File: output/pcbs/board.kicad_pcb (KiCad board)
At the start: 2 copper layers, 94 x 82 mm, 35 parts

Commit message: fillet
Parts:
- added B1: , E73:SW_TACT_ALPS_SKQGABE010, F.Cu at (204.0, 176.5)
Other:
- outline, holes or cut-outs redrawn
- net class Default added: clearance 0.2, trace_width 0.25, via_dia 0.8, via_drill 0.4

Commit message: new footprint
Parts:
- removed B1: , E73:SW_TACT_ALPS_SKQGABE010
- MCU1: value nice_nano -> (none); footprint nice_nano -> ceoloide:mcu_nice_nano
- turned MCU1 to 90 degrees
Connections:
- net P002 renamed MCU1_18
- net P009 renamed MCU1_13
- net P010 renamed MCU1_14
- net P029 renamed MCU1_19
- net P031 renamed MCU1_20
- net P106 renamed MCU1_12
- net P111 renamed MCU1_15
- net P113 renamed MCU1_16
- net P115 renamed MCU1_17
- D1 pad 1: pinky_bottom -> P100
- D1 pad 2: (no net) -> pinky_bottom
- D10 pad 1: index_thumb -> P024
- D10 pad 2: (no net) -> index_thumb
- D11 pad 1: index_bottom -> P100
- D11 pad 2: (no net) -> index_bottom
- D12 pad 1: index_home -> P011
- D12 pad 2: (no net) -> index_home
- D13 pad 1: index_top -> P104
- D13 pad 2: (no net) -> index_top
- D14 pad 1: inner_thumb -> P024
- D14 pad 2: (no net) -> inner_thumb
- D15 pad 1: inner_bottom -> P100
- D15 pad 2: (no net) -> inner_bottom
- D16 pad 1: inner_home -> P011
- D16 pad 2: (no net) -> inner_home
- D17 pad 1: inner_top -> P104
- D17 pad 2: (no net) -> inner_top
- D2 pad 1: pinky_home -> P011
- D2 pad 2: (no net) -> pinky_home
- D3 pad 1: pinky_top -> P104
- D3 pad 2: (no net) -> pinky_top
- D4 pad 1: ring_bottom -> P100
- D4 pad 2: (no net) -> ring_bottom
- D5 pad 1: ring_home -> P011
- D5 pad 2: (no net) -> ring_home
- D6 pad 1: ring_top -> P104
- D6 pad 2: (no net) -> ring_top
- D7 pad 1: middle_bottom -> P100
- D7 pad 2: (no net) -> middle_bottom
- D8 pad 1: middle_home -> P011
- D8 pad 2: (no net) -> middle_home
- D9 pad 1: middle_top -> P104
- D9 pad 2: (no net) -> middle_top
- MCU1 pad 1: P006 -> MCU1_1
- MCU1 pad 10: P011 -> MCU1_10
- MCU1 pad 11: P104 -> MCU1_11
- MCU1 pad 2: P008 -> MCU1_2
- MCU1 pad 21: VCC -> MCU1_21
- MCU1 pad 22: RST -> MCU1_22
- MCU1 pad 23: GND -> MCU1_23
- MCU1 pad 24: RAW -> MCU1_24
- MCU1 pad 3: GND -> MCU1_3
- MCU1 pad 4: GND -> MCU1_4
- MCU1 pad 5: P017 -> MCU1_5
- MCU1 pad 6: P020 -> MCU1_6
- MCU1 pad 7: P022 -> MCU1_7
- MCU1 pad 8: P024 -> MCU1_8
- MCU1 pad 9: P100 -> MCU1_9
- S1 pad 1: (no net) -> P006
- S10 pad 1: (no net) -> P020
- S11 pad 1: (no net) -> P020
- S12 pad 1: (no net) -> P020
- S13 pad 1: (no net) -> P020
- S14 pad 1: (no net) -> P022
- S15 pad 1: (no net) -> P022
- S16 pad 1: (no net) -> P022
- S17 pad 1: (no net) -> P022
- S2 pad 1: (no net) -> P006
- S3 pad 1: (no net) -> P006
- S4 pad 1: (no net) -> P008
- S5 pad 1: (no net) -> P008
- S6 pad 1: (no net) -> P008
- S7 pad 1: (no net) -> P017
- S8 pad 1: (no net) -> P017
- S9 pad 1: (no net) -> P017
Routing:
- net (no net): track 0.00 -> 337.7 mm

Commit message: final
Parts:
- added JST1: , ceoloide:battery_connector_jst_ph_2, F.Cu at (215.0, 160.8)
- added PWR1: , ceoloide:power_switch_smd_side, F.Cu at (206.5, 165.0)
- added RST1: , ceoloide:reset_switch_tht_top, F.Cu at (193.0, 164.3)
- D1, D10, D11, D12, D13, D14, D15, D16, D17, D2, D3, D4, D5, D6, D7, D8, D9: footprint ComboDiode -> ceoloide:diode_tht_sod123; moved to B.Cu
- S1, S10, S11, S12, S13, S14, S15, S16, S17, S2, S3, S4, S5, S6, S7, S8, S9: footprint PG1350 -> ceoloide:switch_gateron_ks27_ks33; moved to B.Cu
- moved D13 13.2 mm to (236.0, 117.8), turned to 90 degrees
- moved D17 13.2 mm to (254.0, 119.8), turned to 90 degrees
- moved D3 13.2 mm to (182.0, 117.8), turned to 90 degrees
- moved D6 13.2 mm to (200.0, 112.8), turned to 90 degrees
- moved D9 13.2 mm to (218.0, 109.8), turned to 90 degrees
- moved D12 12.4 mm to (236.0, 135.8), turned to 90 degrees
- moved D16 12.4 mm to (254.0, 137.8), turned to 90 degrees
- moved D2 12.4 mm to (182.0, 135.8), turned to 90 degrees
- moved D5 12.4 mm to (200.0, 130.8), turned to 90 degrees
- moved D8 12.4 mm to (218.0, 127.8), turned to 90 degrees
- moved D1 11.6 mm to (182.0, 153.8), turned to 90 degrees
- moved D11 11.6 mm to (236.0, 153.8), turned to 90 degrees
- moved D15 11.6 mm to (254.0, 155.8), turned to 90 degrees
- moved D4 11.6 mm to (200.0, 148.8), turned to 90 degrees
- moved D7 11.6 mm to (218.0, 145.8), turned to 90 degrees
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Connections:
- D1 pad 1: P100 -> P14
- D10 pad 1: P024 -> P15
- D11 pad 1: P100 -> P14
- D12 pad 1: P011 -> P16
- D13 pad 1: P104 -> P10
- D14 pad 1: P024 -> P15
- D15 pad 1: P100 -> P14
- D16 pad 1: P011 -> P16
- D17 pad 1: P104 -> P10
- D2 pad 1: P011 -> P16
- D3 pad 1: P104 -> P10
- D4 pad 1: P100 -> P14
- D5 pad 1: P011 -> P16
- D6 pad 1: P104 -> P10
- D7 pad 1: P100 -> P14
- D8 pad 1: P011 -> P16
- D9 pad 1: P104 -> P10
- S1 pad : (no net) -> pinky_bottom
- S1 pad 1: P006 -> P2
- S10 pad : (no net) -> index_thumb
- S10 pad 1: P020 -> P5
- S11 pad : (no net) -> index_bottom
- S11 pad 1: P020 -> P5
- S12 pad : (no net) -> index_home
- S12 pad 1: P020 -> P5
- S13 pad : (no net) -> index_top
- S13 pad 1: P020 -> P5
- S14 pad : (no net) -> inner_thumb
- S14 pad 1: P022 -> P6
- S15 pad : (no net) -> inner_bottom
- S15 pad 1: P022 -> P6
- S16 pad : (no net) -> inner_home
- S16 pad 1: P022 -> P6
- S17 pad : (no net) -> inner_top
- S17 pad 1: P022 -> P6
- S2 pad : (no net) -> pinky_home
- S2 pad 1: P006 -> P2
- S3 pad : (no net) -> pinky_top
- S3 pad 1: P006 -> P2
- S4 pad : (no net) -> ring_bottom
- S4 pad 1: P008 -> P3
- S5 pad : (no net) -> ring_home
- S5 pad 1: P008 -> P3
- S6 pad : (no net) -> ring_top
- S6 pad 1: P008 -> P3
- S7 pad : (no net) -> middle_bottom
- S7 pad 1: P017 -> P4
- S8 pad : (no net) -> middle_home
- S8 pad 1: P017 -> P4
- S9 pad : (no net) -> middle_top
- S9 pad 1: P017 -> P4
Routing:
- net JST1_2: track 0.00 -> 3.60 mm
- net JST1_1: track 0.00 -> 3.60 mm
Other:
- board size 94 x 82 mm -> 94 x 86 mm

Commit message: padding adjust
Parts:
- moved D17 5.00 mm to (258.0, 116.8)
- moved S17 5.00 mm to (251.0, 120.0)
- moved D16 4.47 mm to (258.0, 135.8)
- moved S16 4.47 mm to (251.0, 139.0)
- moved D13 4.24 mm to (239.0, 114.8)
- moved S13 4.24 mm to (232.0, 118.0)
- moved D15 4.12 mm to (258.0, 154.8)
- moved S15 4.12 mm to (251.0, 158.0)
- moved D14 4.00 mm to (258.0, 173.8)
- moved S14 4.00 mm to (251.0, 177.0)
- moved D12 3.61 mm to (239.0, 133.8)
- moved D9 3.61 mm to (220.0, 106.8)
- moved S12 3.61 mm to (232.0, 137.0)
- moved S9 3.61 mm to (213.0, 110.0)
- moved D11 3.16 mm to (239.0, 152.8)
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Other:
- board size 94 x 86 mm -> 99 x 90 mm

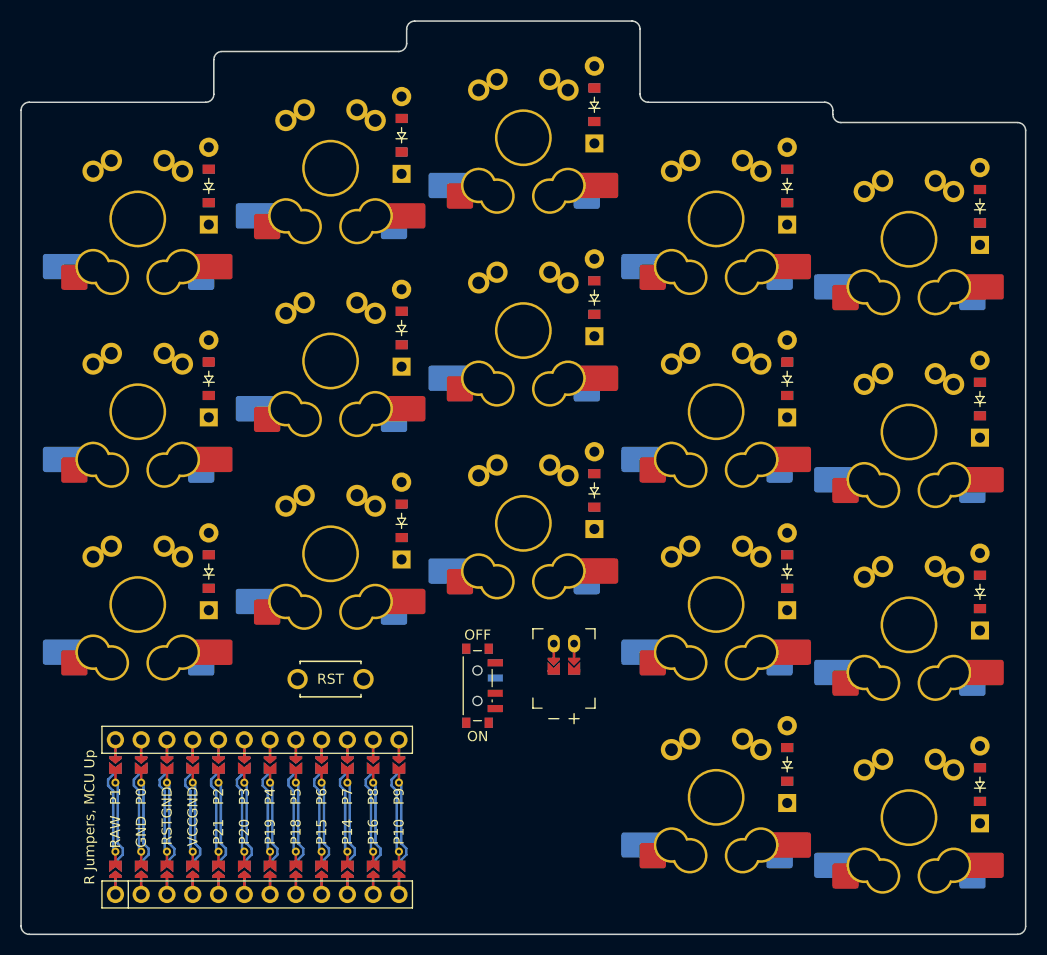
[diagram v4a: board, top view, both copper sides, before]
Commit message: plate update and slim version
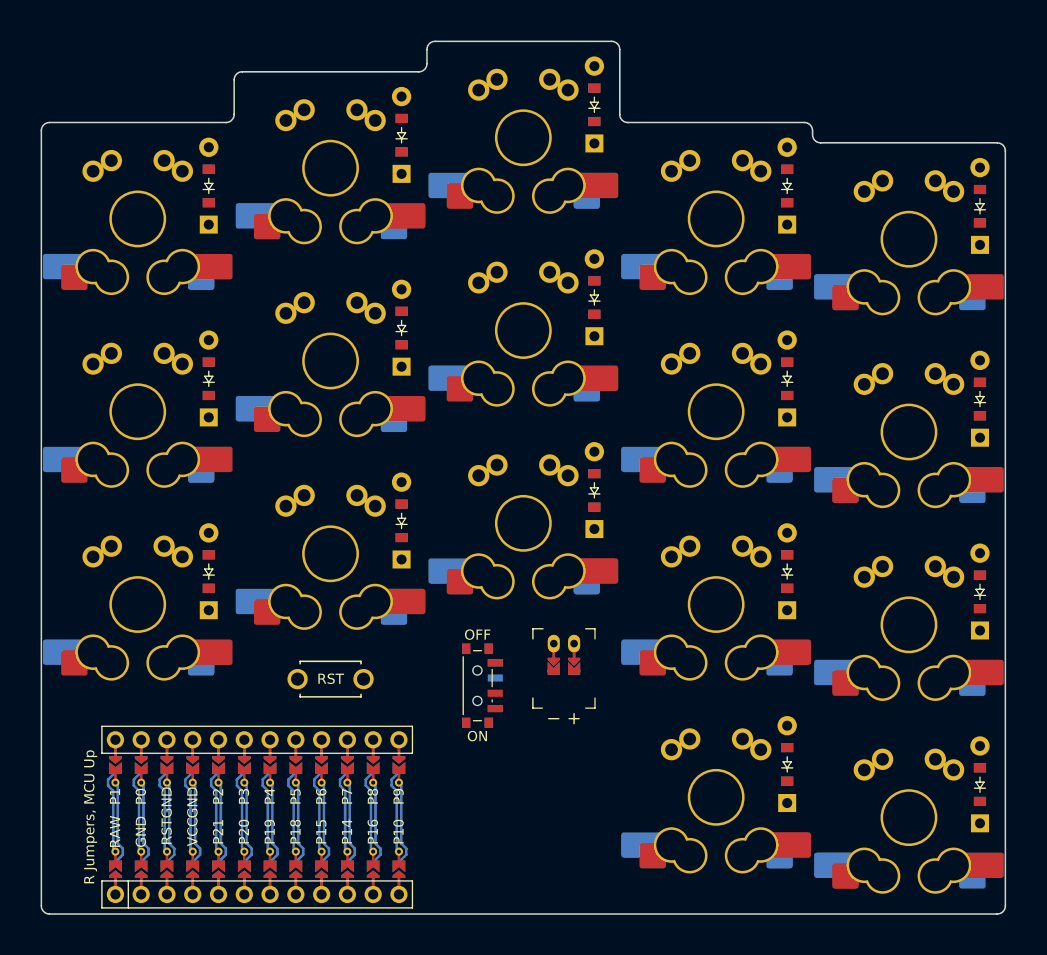
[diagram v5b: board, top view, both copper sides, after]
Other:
- board size 99 x 90 mm -> 95 x 86 mm
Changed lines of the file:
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@@
     (segment (start 218 161.65) (end 218 159.85) (width 0.25) (layer "F.Cu") (net 69))
     (segment (start 218 161.65) (end 218 159.85) (width 0.25) (layer "B.Cu") (net 69))
-  (gr_line (start 262.5 187.7) (end 262.5 109.3) (angle 90) (layer Edge.Cuts) (width 0.15))
-(gr_line (start 164.3 188.5) (end 261.7 188.5) (angle 90) (layer Edge.Cuts) (width 0.15))
-(gr_line (start 163.5 187.7) (end 163.5 107.3) (angle 90) (layer Edge.Cuts) (width 0.15))
-(gr_arc (start 261.7 187.7) (end 261.7 188.5) (angle -90) (layer Edge.Cuts) (width 0.15))
-(gr_arc (start 164.3 187.7) (end 163.5 187.7) (angle -90) (layer Edge.Cuts) (width 0.15))
-(gr_line (start 181.7 106.5) (end 164.3 106.5) (angle 90) (layer Edge.Cuts) (width 0.15))
-(gr_line (start 200.7 101.5) (end 183.3 101.5) (angle 90) (layer Edge.Cuts) (width 0.15))
-(gr_line (start 182.5 102.3) (end 182.5 105.7) (angle 90) (layer Edge.Cuts) (width 0.15))
-(gr_line (start 224.5 105.7) (end 224.5 99.3) (angle 90) (layer Edge.Cuts) (width 0.15))
-(gr_line (start 223.7 98.5) (end 202.3 98.5) (angle 90) (layer Edge.Cuts) (width 0.15))
-(gr_line (start 201.5 99.3) (end 201.5 100.7) (angle 90) (layer Edge.Cuts) (width 0.15))
-(gr_line (start 243.5 107.7) (end 243.5 107.3) (angle 90) (layer Edge.Cuts) (width 0.15))
-(gr_line (start 242.7 106.5) (end 225.3 106.5) (angle 90) (layer Edge.Cuts) (width 0.15))
-(gr_line (start 261.7 108.5) (end 244.3 108.5) (angle 90) (layer Edge.Cuts) (width 0.15))
-(gr_arc (start 261.7 109.3) (end 262.5 109.3) (angle -90) (layer Edge.Cuts) (width 0.15))
-(gr_arc (start 244.3 107.7) (end 243.5 107.7) (angle -90) (layer Edge.Cuts) (width 0.15))
-(gr_arc (start 242.7 107.3) (end 243.5 107.3) (angle -90) (layer Edge.Cuts) (width 0.15))
-(gr_arc (start 225.3 105.7) (end 224.5 105.7) (angle -90) (layer Edge.Cuts) (width 0.15))
-(gr_arc (start 223.7 99.3) (end 224.5 99.3) (angle -90) (layer Edge.Cuts) (width 0.15))
-(gr_arc (start 202.3 99.3) (end 202.3 98.5) (angle -90) (layer Edge.Cuts) (width 0.15))
-(gr_arc (start 200.7 100.7) (end 200.7 101.5) (angle -90) (layer Edge.Cuts) (width 0.15))
-(gr_arc (start 183.3 102.3) (end 183.3 101.5) (angle -90) (layer Edge.Cuts) (width 0.15))
-(gr_arc (start 181.7 105.7) (end 181.7 106.5) (angle -90) (layer Edge.Cuts) (width 0.15))
-(gr_arc (start 164.3 107.3) (end 164.3 106.5) (angle -90) (layer Edge.Cuts) (width 0.15))
+  (gr_line (start 260.5 185.7) (end 260.5 111.3) (angle 90) (layer Edge.Cuts) (width 0.15))
+(gr_line (start 166.3 186.5) (end 259.7 186.5) (angle 90) (layer Edge.Cuts) (width 0.15))
+(gr_line (start 165.5 185.7) (end 165.5 109.3) (angle 90) (layer Edge.Cuts) (width 0.15))
+(gr_arc (start 259.7 185.7) (end 259.7 186.5) (angle -90) (layer Edge.Cuts) (width 0.15))
+(gr_arc (start 166.3 185.7) (end 165.5 185.7) (angle -90) (layer Edge.Cuts) (width 0.15))
+(gr_line (start 183.7 108.5) (end 166.3 108.5) (angle 90) (layer Edge.Cuts) (width 0.15))
+(gr_line (start 202.7 103.5) (end 185.3 103.5) (angle 90) (layer Edge.Cuts) (width 0.15))
+(gr_line (start 184.5 104.3) (end 184.5 107.7) (angle 90) (layer Edge.Cuts) (width 0.15))
+(gr_line (start 222.5 107.7) (end 222.5 101.3) (angle 90) (layer Edge.Cuts) (width 0.15))
+(gr_line (start 221.7 100.5) (end 204.3 100.5) (angle 90) (layer Edge.Cuts) (width 0.15))
+(gr_line (start 203.5 101.3) (end 203.5 102.7) (angle 90) (layer Edge.Cuts) (width 0.15))
+(gr_line (start 241.5 109.7) (end 241.5 109.3) (angle 90) (layer Edge.Cuts) (width 0.15))
+(gr_line (start 240.7 108.5) (end 223.3 108.5) (angle 90) (layer Edge.Cuts) (width 0.15))
+(gr_line (start 259.7 110.5) (end 242.3 110.5) (angle 90) (layer Edge.Cuts) (width 0.15))
+(gr_arc (start 259.7 111.3) (end 260.5 111.3) (angle -90) (layer Edge.Cuts) (width 0.15))
+(gr_arc (start 242.3 109.7) (end 241.5 109.7) (angle -90) (layer Edge.Cuts) (width 0.15))
+(gr_arc (start 240.7 109.3) (end 241.5 109.3) (angle -90) (layer Edge.Cuts) (width 0.15))
+(gr_arc (start 223.3 107.7) (end 222.5 107.7) (angle -90) (layer Edge.Cuts) (width 0.15))
+(gr_arc (start 221.7 101.3) (end 222.5 101.3) (angle -90) (layer Edge.Cuts) (width 0.15))
+(gr_arc (start 204.3 101.3) (end 204.3 100.5) (angle -90) (layer Edge.Cuts) (width 0.15))
+(gr_arc (start 202.7 102.7) (end 202.7 103.5) (angle -90) (layer Edge.Cuts) (width 0.15))
+(gr_arc (start 185.3 104.3) (end 185.3 103.5) (angle -90) (layer Edge.Cuts) (width 0.15))
+(gr_arc (start 183.7 107.7) (end 183.7 108.5) (angle -90) (layer Edge.Cuts) (width 0.15))
+(gr_arc (start 166.3 109.3) (end 166.3 108.5) (angle -90) (layer Edge.Cuts) (width 0.15))
 )

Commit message: mk12 config
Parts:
- moved D17 5.00 mm to (254.0, 119.8)
- moved S17 5.00 mm to (247.0, 123.0)
- moved D16 4.47 mm to (254.0, 137.8)
- moved S16 4.47 mm to (247.0, 141.0)
- moved D13 4.24 mm to (236.0, 117.8)
- moved S13 4.24 mm to (229.0, 121.0)
- moved D15 4.12 mm to (254.0, 155.8)
- moved S15 4.12 mm to (247.0, 159.0)
- moved D14 4.00 mm to (254.0, 173.8)
- moved S14 4.00 mm to (247.0, 177.0)
- moved D12 3.61 mm to (236.0, 135.8)
- moved D9 3.61 mm to (218.0, 109.8)
- moved S12 3.61 mm to (229.0, 139.0)
- moved S9 3.61 mm to (211.0, 113.0)
- moved D11 3.16 mm to (236.0, 153.8)
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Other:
- board size 95 x 86 mm -> 90 x 82 mm

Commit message: mk3 pcb donw
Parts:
- added H1: , ceoloide:mounting_hole_plated, F.Cu at (184.5, 113.2)
- added H2: , ceoloide:mounting_hole_plated, F.Cu at (184.5, 151.2)
- added H3: , ceoloide:mounting_hole_plated, F.Cu at (241.5, 115.2)
- added H4: , ceoloide:mounting_hole_plated, F.Cu at (241.5, 174.2)
- moved RST1 31.2 mm to (218.0, 183.0)
- moved PWR1 18.0 mm to (207.0, 183.0), turned to -90 degrees
- moved D3 8.87 mm to (175.0, 112.3), turned to 0 degrees
- moved D2 8.29 mm to (175.0, 131.3), turned to 0 degrees
- moved D6 8.11 mm to (194.0, 107.3), turned to 0 degrees
- moved D1 7.80 mm to (175.0, 150.3), turned to 0 degrees
- moved JST1 7.75 mm to (218.0, 168.0)
- moved D5 7.47 mm to (194.0, 126.3), turned to 0 degrees
- moved D9 7.40 mm to (213.0, 104.3), turned to 0 degrees
- moved D4 6.92 mm to (194.0, 145.3), turned to 0 degrees
- moved D13 6.76 mm to (232.0, 112.3), turned to 0 degrees
- moved D8 6.69 mm to (213.0, 123.3), turned to 0 degrees
- moved D17 6.22 mm to (251.0, 114.3), turned to 0 degrees
- moved D7 6.07 mm to (213.0, 142.3), turned to 0 degrees
- moved D12 5.98 mm to (232.0, 131.3), turned to 0 degrees
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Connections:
- D1 pad 1: P14 -> P16
- D10 pad 1: P15 -> P10
- D11 pad 1: P14 -> P16
- D12 pad 1: P16 -> P14
- D13 pad 1: P10 -> P15
- D14 pad 1: P15 -> P10
- D15 pad 1: P14 -> P16
- D16 pad 1: P16 -> P14
- D17 pad 1: P10 -> P15
- D2 pad 1: P16 -> P14
- D3 pad 1: P10 -> P15
- D4 pad 1: P14 -> P16
- D5 pad 1: P16 -> P14
- D6 pad 1: P10 -> P15
- D7 pad 1: P14 -> P16
- D8 pad 1: P16 -> P14
- D9 pad 1: P10 -> P15
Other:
- board size 90 x 82 mm -> 95 x 86 mm

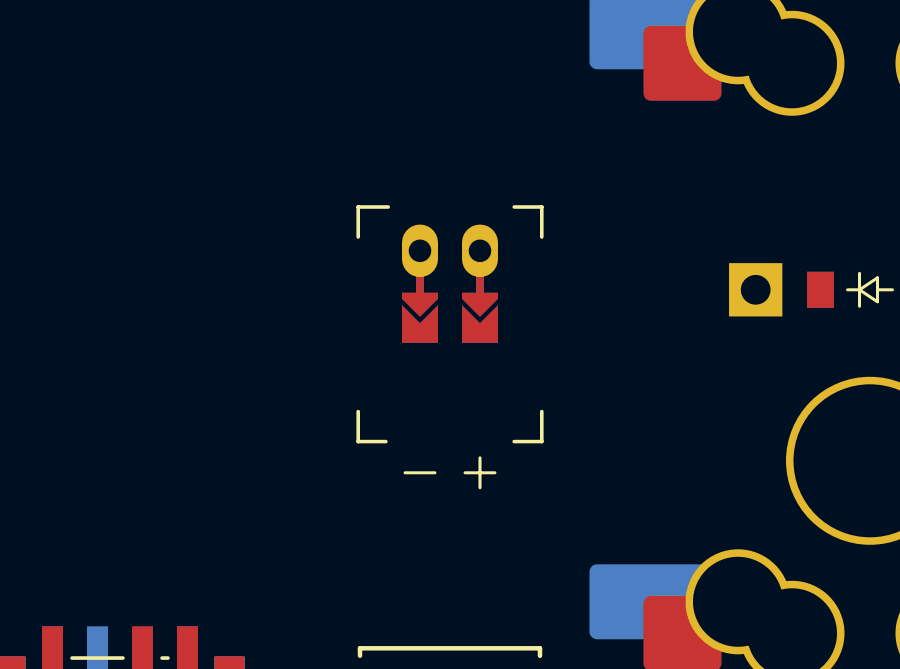
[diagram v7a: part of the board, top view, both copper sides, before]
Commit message: battery connector change
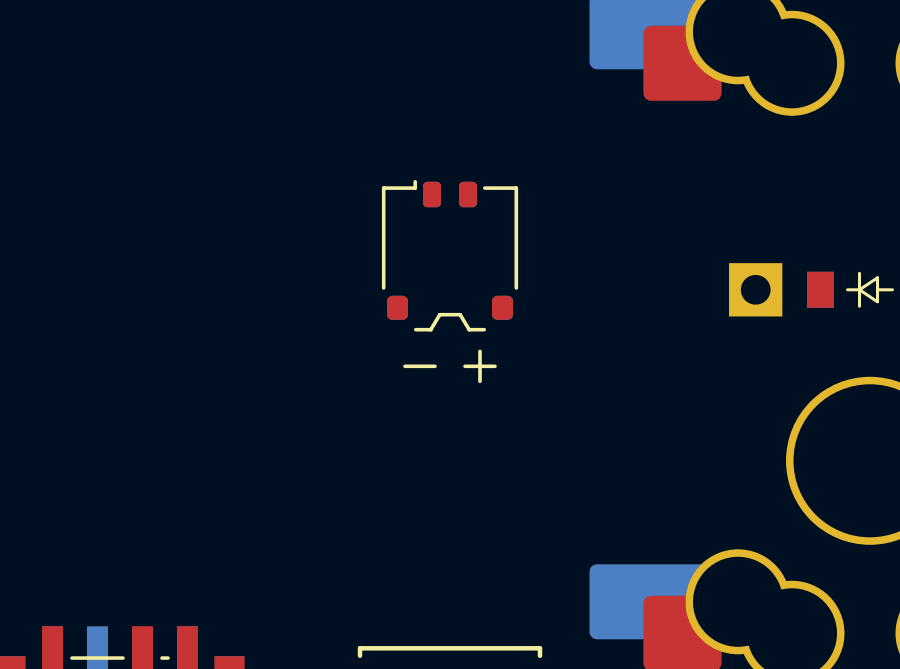
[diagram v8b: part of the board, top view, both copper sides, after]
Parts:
- removed JST1: , ceoloide:battery_connector_jst_ph_2
- added CONN1: , ceoloide:battery_connector_molex_pico_ezmate_1x02, F.Cu at (218.0, 168.0)
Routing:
- net JST1_2: track 3.60 -> 0.00 mm
- net JST1_1: track 3.60 -> 0.00 mm
